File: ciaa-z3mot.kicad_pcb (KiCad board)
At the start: 2 copper layers, 18.8 x 67.7 mm, 78 parts, among them J1 Conn_01x20, J2 Conn_01x20, J3 Conn_01x02, J4 SWD, J5 Conn_01x04, J6 Conn_Coaxial, J7 Conn_01x05, J8 Conn_Coaxial, SW1 reset, SW2 reset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

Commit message: Edición readme
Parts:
- moved L1 0.37 mm to (131.8, 88.9)

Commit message: more readme!!! ):
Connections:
- BT1 pad 3: (no net) -> GND
- U1 pad : (no net) -> GND
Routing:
- net GND: track 239.3 -> 251.7 mm
- net +3V3: track 95.5 -> 99.0 mm
- net /PC10: track 15.8 -> 17.6 mm
- net HFXTAL_P: track 7.78 -> 9.55 mm
- net /nRESET: track 61.2 -> 63.0 mm
- net /PF5: track 1.40 -> 3.17 mm
- net /PF4: track 14.0 -> 15.8 mm
- net /PF2: track 19.7 -> 21.4 mm
- net /PF1/SWDIO: track 25.9 -> 27.7 mm
- net /PF0/SWCLK: track 28.0 -> 29.8 mm
- net /PE12: track 5.41 -> 7.18 mm
- net /PD7: track 9.30 -> 11.1 mm
- net /PD6: track 7.07 -> 8.84 mm
- net /PD5: track 4.88 -> 6.65 mm
- net /PC9: track 13.6 -> 15.3 mm
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
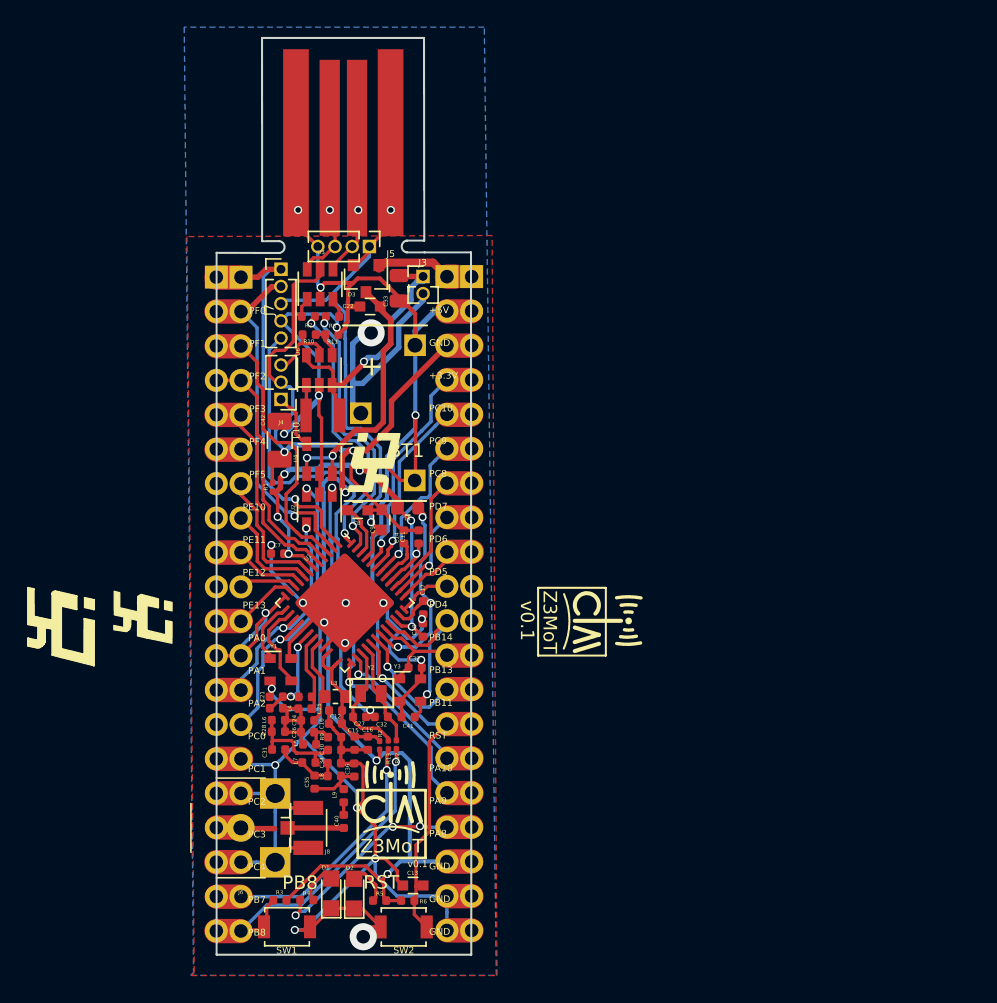
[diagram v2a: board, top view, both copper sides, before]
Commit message: BOM
edicion de fb mdp1640 y en el bom
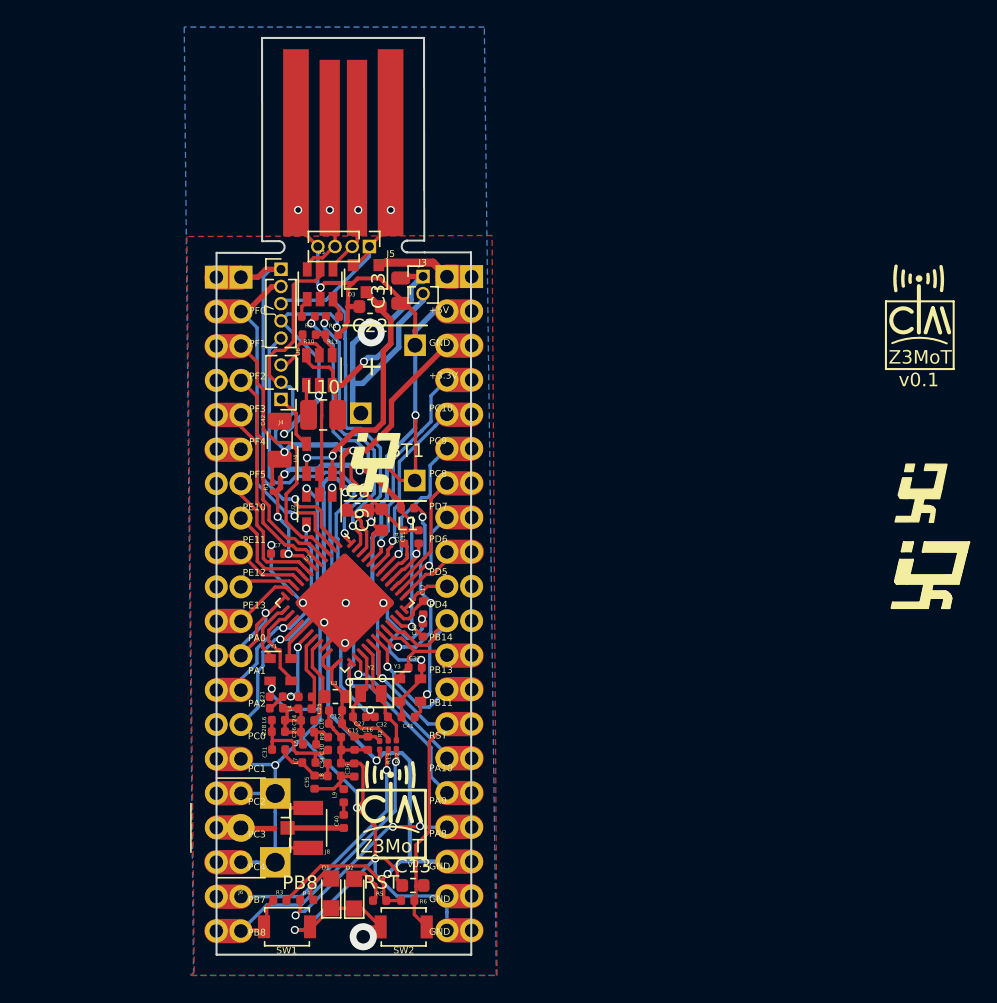
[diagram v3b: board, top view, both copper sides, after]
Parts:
- C10: value 100n -> 100p
- C12, C24, C40: value 100n -> 470p
- C13, C22, C8, C9: footprint footprints:C_0603 -> Capacitor_SMD:C_0603_1608Metric
- C16: value 100n -> 1u
- C17, C18: value 10u -> 100n
- C21: value 100n -> 12p
- C25: value 100n -> 6.2p
- C26, C36: value 100n -> 11p
- C27, C32: value 1u -> 12.5p
- C28: value 100n -> NM
- C30, C34: value 100n -> 18p
- C31: value 100n -> 3p
- C35: value 100n -> 2p
- C39, C41: value 1u -> 10p
- C42: value 4.7u -> 10u
- L1: footprint Inductor_SMD:L_0603_1608Metric -> Inductor_SMD:L_0402_1005Metric
- L10: value L_Core_Iron -> 4.7uH; footprint Inductor_SMD:L_Taiyo-Yuden_MD-4040 -> Inductor_SMD:L_1008_2520Metric
- L2: value L -> 220nH
- L3: value L -> 390nH
- L4: value L -> 150nH
- L5: value L -> 82nH
- L6, L8: value L -> 47nH
- L7: value L -> 68nH
- L9: value L -> 27nH
- R1, R2: value 0R -> 1R
- R9: value 1K -> 50R
- moved C33 0.21 mm to (131.3, 72.8)
- moved L10 0.14 mm to (125.6, 82.0)
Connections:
- BT1 pad 3: GND -> (no net)
- U1 pad : GND -> (no net)
